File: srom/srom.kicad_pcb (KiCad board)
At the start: 2 copper layers, 83.3 x 76.1 mm, 18 parts, among them J1 Conn_01x03_Female, U1 4075, U2 74LS245, U3 74LS245, U4 74LS245, U5 Pico-rp2040

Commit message: minor updates to layout
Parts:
- added 1: , , F.Cu at (97.0, 118.9)
- added 10: , , F.Cu at (94.4, 124.0)
- added 11: , , F.Cu at (97.0, 124.0)
- added 12: , , F.Cu at (99.5, 124.0)
- added 13: , , F.Cu at (102.1, 116.3)
- added 13: , , F.Cu at (102.0, 124.0)
- added 14: , , F.Cu at (104.6, 116.3)
- added 14: , , F.Cu at (104.6, 124.0)
- added 2: , , F.Cu at (99.5, 118.9)
- added 3: , , F.Cu at (102.1, 111.2)
- added 3: , , F.Cu at (102.0, 118.9)
- added 4: , , F.Cu at (104.6, 111.2)
- added 4: , , F.Cu at (104.6, 118.9)
- added 5: , , F.Cu at (94.4, 121.4)
- added 6: , , F.Cu at (97.0, 121.4)
- added 7: , , F.Cu at (99.5, 121.4)
- added 8: , , F.Cu at (102.1, 113.8)
- added 8: , , F.Cu at (102.0, 121.4)
- added 9: , , F.Cu at (104.6, 121.4)
- added 9: , , F.Cu at (104.6, 113.8)
- added ?: , , F.Cu at (101.8, 54.6)
- added ?: , , F.Cu at (99.7, 52.6)
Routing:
- net unconnected-(U5-Pad32): track 0.00 -> 28.1 mm
- net unconnected-(U5-Pad34): track 0.00 -> 25.4 mm
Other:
- board text added: "GND"
- board text added: "GPIO27"
- board text added: "GPIO28"

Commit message: fab1.0 ready to go
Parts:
- added ?: , , F.Cu at (62.8, 107.2)
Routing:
- net GND: vias 18 -> 19
- added copper zone on F.Cu, net GND
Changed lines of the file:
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@@
       (layerselection 0x00010fc_ffffffff)
       (disableapertmacros false)
-      (usegerberextensions false)
-      (usegerberattributes true)
-      (usegerberadvancedattributes true)
-      (creategerberjobfile true)
+      (usegerberextensions true)
+      (usegerberattributes false)
+      (usegerberadvancedattributes false)
+      (creategerberjobfile false)
       (svguseinch false)
       (svgprecision 6)
@@
       (psa4output false)
       (plotreference true)
-      (plotvalue true)
+      (plotvalue false)
       (plotinvisibletext false)
       (sketchpadsonfab false)
-      (subtractmaskfromsilk false)
+      (subtractmaskfromsilk true)
       (outputformat 1)
       (mirror false)
-      (drillshape 1)
+      (drillshape 0)
       (scaleselection 1)
-      (outputdirectory "")
+      (outputdirectory "fab1.0")
     )
   )
@@
     (fp_line (start 1.6 0.8) (end -1.6 0.8) (layer "F.Fab") (width 0.1))
     (fp_line (start -1.6 -0.8) (end 1.6 -0.8) (layer "F.Fab") (width 0.1))
-    (pad "1" smd roundrect (at -1.475 0) (size 1.15 1.8) (layers "F.Cu" "F.Paste" "F.Mask") (roundrect_rratio 0.217391)
+    (pad "1" smd roundrect (at -1.475 0) (size 1.15 1.8) (layers "F.Cu" "F.Paste" "F.Mask") (roundrect_rratio 0.2173913043)
       (net 2 "GND") (pintype "passive"))
-    (pad "2" smd roundrect (at 1.475 0) (size 1.15 1.8) (layers "F.Cu" "F.Paste" "F.Mask") (roundrect_rratio 0.217391)
+    (pad "2" smd roundrect (at 1.475 0) (size 1.15 1.8) (layers "F.Cu" "F.Paste" "F.Mask") (roundrect_rratio 0.2173913043)
       (net 1 "+3V3") (pintype "passive"))
     (model "${KICAD6_3DMODEL_DIR}/Capacitor_SMD.3dshapes/C_1206_3216Metric.wrl"
@@
     (fp_line (start 1.6 0.8) (end -1.6 0.8) (layer "F.Fab") (width 0.1))
     (fp_line (start 1.6 -0.8) (end 1.6 0.8) (layer "F.Fab") (width 0.1))
-    (pad "1" smd roundrect (at -1.475 0 270) (size 1.15 1.8) (layers "F.Cu" "F.Paste" "F.Mask") (roundrect_rratio 0.217391)
+    (pad "1" smd roundrect (at -1.475 0 270) (size 1.15 1.8) (layers "F.Cu" "F.Paste" "F.Mask") (roundrect_rratio 0.2173913043)
       (net 3 "+5V") (pintype "passive"))
-    (pad "2" smd roundrect (at 1.475 0 270) (size 1.15 1.8) (layers "F.Cu" "F.Paste" "F.Mask") (roundrect_rratio 0.217391)
+    (pad "2" smd roundrect (at 1.475 0 270) (size 1.15 1.8) (layers "F.Cu" "F.Paste" "F.Mask") (roundrect_rratio 0.2173913043)
       (net 2 "GND") (pintype "passive"))
     (model "${KICAD6_3DMODEL_DIR}/Capacitor_SMD.3dshapes/C_1206_3216Metric.wrl"
@@
     (fp_line (start 1.6 -0.8) (end 1.6 0.8) (layer "F.Fab") (width 0.1))
     (fp_line (start -1.6 0.8) (end -1.6 -0.8) (layer "F.Fab") (width 0.1))
-    (pad "1" smd roundrect (at -1.475 0 180) (size 1.15 1.8) (layers "F.Cu" "F.Paste" "F.Mask") (roundrect_rratio 0.217391)
+    (pad "1" smd roundrect (at -1.475 0 180) (size 1.15 1.8) (layers "F.Cu" "F.Paste" "F.Mask") (roundrect_rratio 0.2173913043)
       (net 1 "+3V3") (pintype "passive"))
-    (pad "2" smd roundrect (at 1.475 0 180) (size 1.15 1.8) (layers "F.Cu" "F.Paste" "F.Mask") (roundrect_rratio 0.217391)
+    (pad "2" smd roundrect (at 1.475 0 180) (size 1.15 1.8) (layers "F.Cu" "F.Paste" "F.Mask") (roundrect_rratio 0.2173913043)
       (net 2 "GND") (pintype "passive"))
     (model "${KICAD6_3DMODEL_DIR}/Capacitor_SMD.3dshapes/C_1206_3216Metric.wrl"
@@
   )
   (footprint "" (layer "F.Cu")
+    (at 62.77 107.21)
+    (fp_text reference "" (at 0 0) (layer "F.SilkS")
+      (effects (font (size 1.27 1.27) (thickness 0.15)))
+    )
+    (fp_text value "" (at 0 0) (layer "F.SilkS")
+      (effects (font (size 1.27 1.27) (thickness 0.15)))
+    )
+    (pad "" thru_hole circle (at 0 0) (size 2 2) (drill 1) (layers *.Cu *.Mask)
+      (net 2 "GND"))
+  )
+  (footprint "" (layer "F.Cu")
     (at 99.73 52.6)
     (fp_text reference "" (at 0 0) (layer "F.SilkS")
@@
     (fp_line (start -1.6 -0.8) (end 1.6 -0.8) (layer "F.Fab") (width 0.1))
     (fp_line (start -1.6 0.8) (end -1.6 -0.8) (layer "F.Fab") (width 0.1))
-    (pad "1" smd roundrect (at -1.475 0 180) (size 1.15 1.8) (layers "F.Cu" "F.Paste" "F.Mask") (roundrect_rratio 0.217391)
+    (pad "1" smd roundrect (at -1.475 0 180) (size 1.15 1.8) (layers "F.Cu" "F.Paste" "F.Mask") (roundrect_rratio 0.2173913043)
       (net 1 "+3V3") (pintype "passive"))
-    (pad "2" smd roundrect (at 1.475 0 180) (size 1.15 1.8) (layers "F.Cu" "F.Paste" "F.Mask") (roundrect_rratio 0.217391)
+    (pad "2" smd roundrect (at 1.475 0 180) (size 1.15 1.8) (layers "F.Cu" "F.Paste" "F.Mask") (roundrect_rratio 0.2173913043)
       (net 2 "GND") (pintype "passive"))
     (model "${KICAD6_3DMODEL_DIR}/Capacitor_SMD.3dshapes/C_1206_3216Metric.wrl"
@@
   (gr_line (start 95.03 53.86) (end 95.53 53.52) (layer "F.SilkS") (width 0.15))
   (gr_line (start 95.03 53.18) (end 95.03 53.86) (layer "F.SilkS") (width 0.15))
+  (gr_rect (start 91.9 125.49) (end 70.19 123.34) (layer "B.Mask") (width 0.15) (fill solid))
+  (gr_rect (start 91.93 125.49) (end 70.21 123.57) (layer "F.Mask") (width 0.15) (fill solid))
   (gr_rect (start 23.18 49.98) (end 106.46 126.07) (layer "Edge.Cuts") (width 0.1) (fill none))
   (gr_text "GPIO28" (at 102.36 52.05) (layer "F.SilkS")
@@
   )
   (gr_text "ROM Acc\n3V3" (at 71.52 83.08) (layer "F.SilkS")
+    (effects (font (size 1 0.5) (thickness 0.125)))
+  )
+  (gr_text "GND" (at 60.55 107.29) (layer "F.SilkS")
     (effects (font (size 1 0.5) (thickness 0.125)))
   )
@@
   (via (at 72.48 80.34) (size 0.8) (drill 0.4) (layers "F.Cu" "B.Cu") (net 2))
   (via (at 41.29 88.31) (size 0.8) (drill 0.4) (layers "F.Cu" "B.Cu") (net 2))
+  (via (at 73.44 124.94) (size 0.8) (drill 0.4) (layers "F.Cu" "B.Cu") (free) (net 2))
   (via (at 58.31 54.81) (size 0.8) (drill 0.4) (layers "F.Cu" "B.Cu") (net 2))
   (via (at 71.69 112.51) (size 0.8) (drill 0.4) (layers "F.Cu" "B.Cu") (net 2))
@@
   (segment (start 101.94 57.39) (end 99.14 54.59) (width 0.25) (layer "B.Cu") (net 85))
   (segment (start 99.14 54.59) (end 99.14 53.19) (width 0.25) (layer "B.Cu") (net 85))
-  (segment (start 99.81 52.68) (end 99.73 52.6) (width 0.25) (layer "B.Cu") (net 85))
   (segment (start 99.14 53.19) (end 99.73 52.6) (width 0.25) (layer "B.Cu") (net 85))
   (segment (start 100.69 73.43) (end 101.94 72.18) (width 0.25) (layer "B.Cu") (net 85))
   (segment (start 98.13 73.43) (end 100.69 73.43) (width 0.25) (layer "B.Cu") (net 85))
+  (zone (net 2) (net_name "GND") (layers F&B.Cu) (hatch edge 0.508)
+    (connect_pads (clearance 0.508))
+    (min_thickness 0.254) (filled_areas_thickness no)
+    (fill yes (thermal_gap 0.508) (thermal_bridge_width 0.508))
+    (polygon
+      (pts
+        (xy 91.42 123.47)
+        (xy 91.42 126.43)
+        (xy 91.341525 125.611093)
+        (xy 70.219569 125.566897)
+        (xy 70.278044 123.455804)
+      )
+    )
+  )
+  (zone (net 2) (net_name "GND") (layers F&B.Cu) (hatch edge 0.508)
+    (connect_pads (clearance 0.508))
+    (min_thickness 0.254) (filled_areas_thickness no)
+    (fill yes (thermal_gap 0.508) (thermal_bridge_width 0.508))
+    (polygon
+      (pts
+        (xy 91.787252 125.538043)
+        (xy 70.257252 125.588043)
+        (xy 70.26 123.511551)
+        (xy 70.29 123.651551)
+        (xy 70.260167 123.461569)
+        (xy 91.790167 123.441569)
+      )
+    )
+  )
   (zone (net 2) (net_name "GND") (layer "B.Cu") (hatch edge 0.508)
     (connect_pads (clearance 0.508))

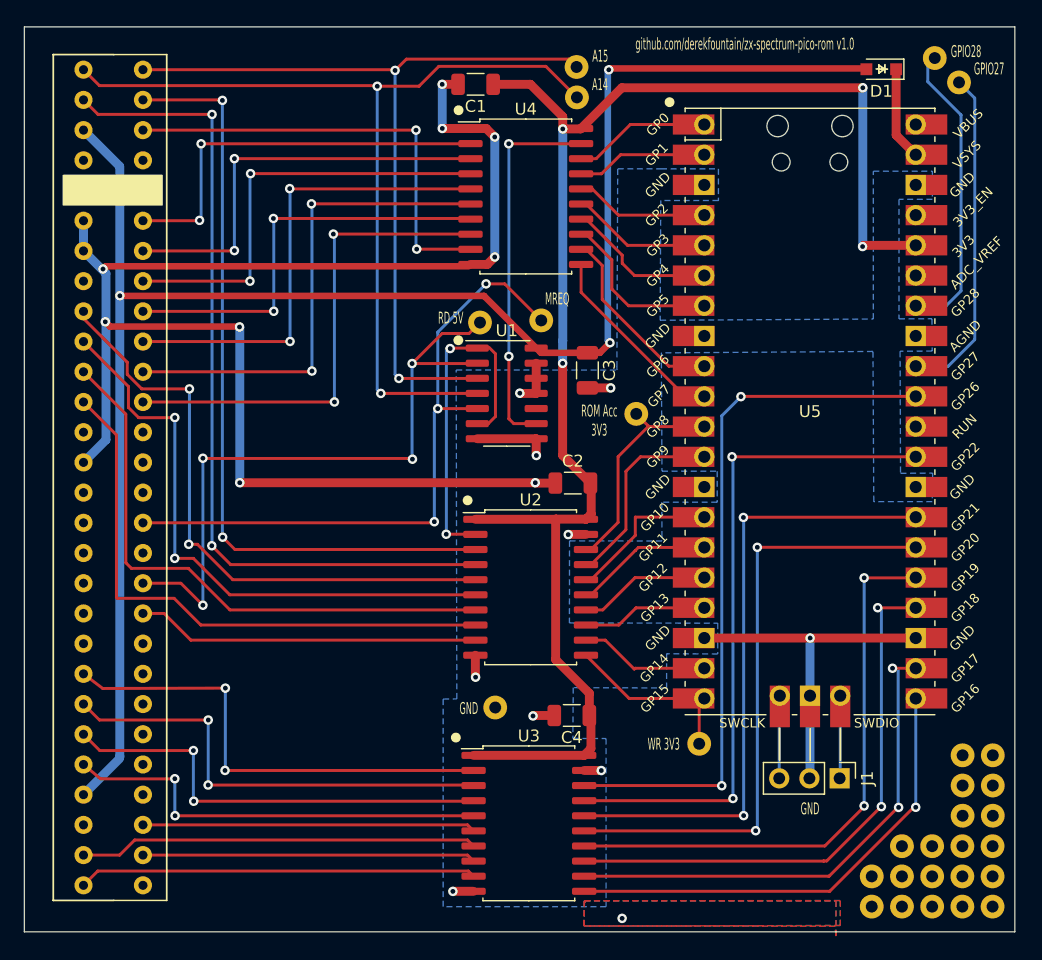
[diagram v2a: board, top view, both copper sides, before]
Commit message: update pcb with errata
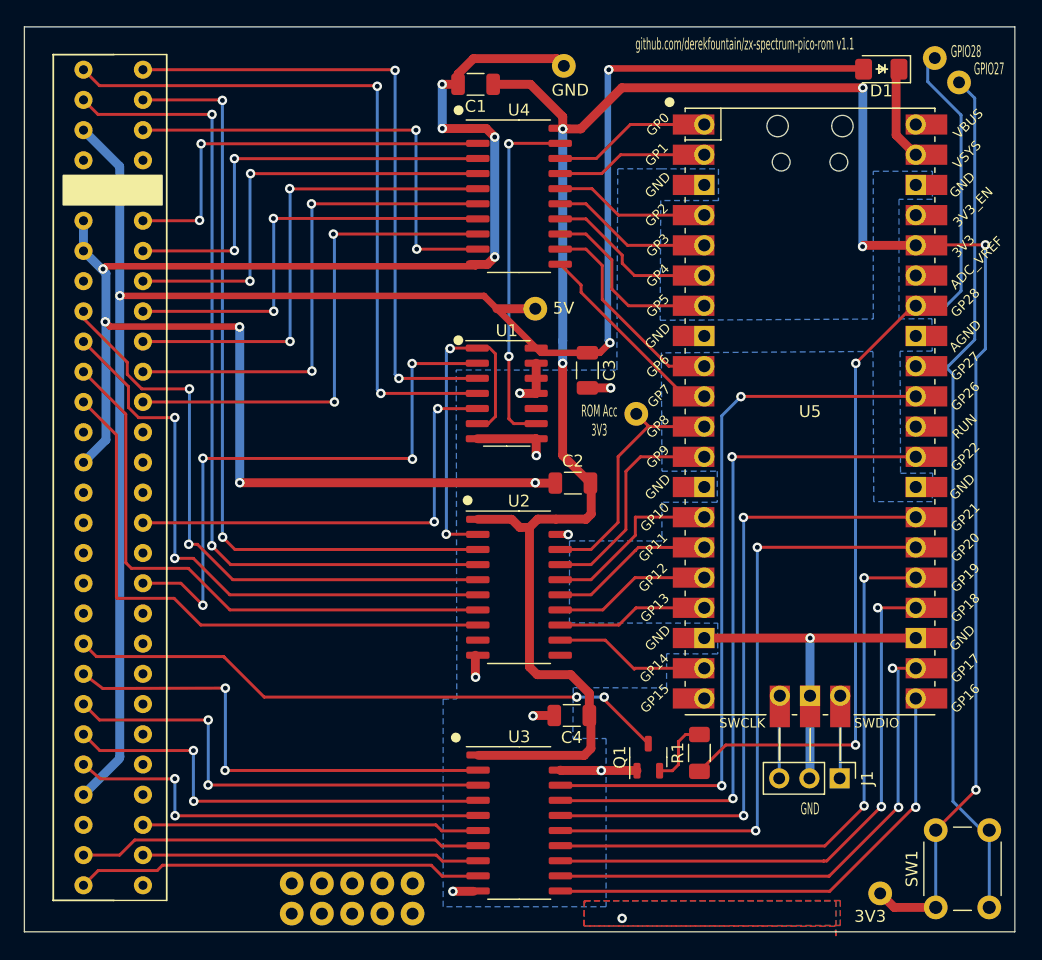
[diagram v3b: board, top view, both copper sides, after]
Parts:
- removed 1, 2, 3 (x2), 4 (x2): , 
- removed the 13 at (102.1, 116.3)
- removed the 14 at (104.6, 116.3)
- removed the 8 at (102.1, 113.8)
- removed the 9 at (104.6, 113.8)
- removed the ? at (61.5, 74.8)
- removed the ? at (66.6, 74.7)
- removed the ? at (69.6, 55.9)
- removed the ? at (62.8, 107.2)
- removed the ? at (79.9, 110.3)
- removed the ? at (69.6, 53.4)
- added 14: , , F.Cu at (95.1, 122.8)
- added 14: , , F.Cu at (68.5, 53.3)
- added ?: , , F.Cu at (66.1, 73.7)
- added Q1: PN2222A, Package_TO_SOT_SMD:SOT-23-3, F.Cu at (75.6, 111.4)
- added R1: 1K, Resistor_SMD:R_1206_3216Metric_Pad1.30x1.75mm_HandSolder, F.Cu at (79.9, 111.0)
- added SW1: SW_SPST, Button_Switch_THT:SW_PUSH_6mm_H4.3mm, F.Cu at (99.8, 124.0)
- D1: footprint Diode_SMD:D_SOD-323_HandSoldering -> Diode_SMD:D_1206_3216Metric_Pad1.42x1.75mm_HandSolder
- U2, U3, U4: footprint Package_SO:SOIC-20W_7.5x12.8mm_P1.27mm -> Package_SO:SO-20_5.3x12.6mm_P1.27mm
- moved 10 48.8 mm to (45.7, 124.5)
- moved 5 48.8 mm to (45.7, 122.0)
- moved 12 48.8 mm to (50.7, 124.5)
- moved 14 48.8 mm to (55.8, 124.5)
- moved 7 48.8 mm to (50.7, 122.0)
- moved 9 48.8 mm to (55.8, 122.0)
- moved 11 48.8 mm to (48.2, 124.5)
- moved 13 48.8 mm to (53.3, 124.5)
- moved 6 48.8 mm to (48.2, 122.0)
- moved 8 48.8 mm to (53.3, 122.0)
- moved U2 0.98 mm to (64.8, 97.1)
- moved U3 0.81 mm to (64.8, 116.9)
- moved U4 0.57 mm to (64.8, 64.2)
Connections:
- U2 pad 11: WR -> unconnected-(U2-Pad11)
- U2 pad 9: ZXWR -> unconnected-(U2-Pad9)
- U5 pad 20: WR -> unconnected-(U5-Pad20)
- U5 pad 32: unconnected-(U5-Pad32) -> PICO_USER_INPUT
- U5 pad 34: unconnected-(U5-Pad34) -> PICO_RESET_Z80
- Z1 pad A19: ZXWR -> unconnected-(Z1-PadA19)
- Z1 pad B20: unconnected-(Z1-PadB20) -> ZXRESET
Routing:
- net PICO_RESET_Z80: track 0.00 -> 77.7 mm, vias 0 -> 2
- net PICO_USER_INPUT: track 0.00 -> 75.5 mm
- net +3V3: track 126.5 -> 196.8 mm, vias 4 -> 6
- net ZXRESET: track 0.00 -> 51.1 mm, vias 0 -> 2
- net ZXWR: track 28.9 -> 0.00 mm
- net unconnected-(U5-Pad32): track 28.1 -> 0.00 mm
- net unconnected-(U5-Pad34): track 25.3 -> 0.00 mm
- net ZXA14: track 77.9 -> 59.3 mm
- net ZXMREQ: track 55.6 -> 37.5 mm, vias 3 -> 2
- net ZXA15: track 69.8 -> 53.9 mm
- net WR: track 15.4 -> 0.00 mm
- net GND: track 176.2 -> 191.6 mm
- net ZXRD: track 56.3 -> 49.1 mm
- net Net-(Q1-Pad2): track 0.00 -> 5.75 mm
- net +5V: track 146.7 -> 149.9 mm
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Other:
- board text added: "3V3"
- board text added: "5V"
- board text added: "github.com/derekfountain/zx-spectrum-pico-rom v1.1"
- board text removed: "A14"
- board text removed: "A15"
- board text removed: "MREQ"
- board text removed: "RD 5V"
- board text removed: "WR 3V3"
- board text removed: "github.com/derekfountain/zx-spectrum-pico-rom v1.0"

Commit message: add a ground plane on the back
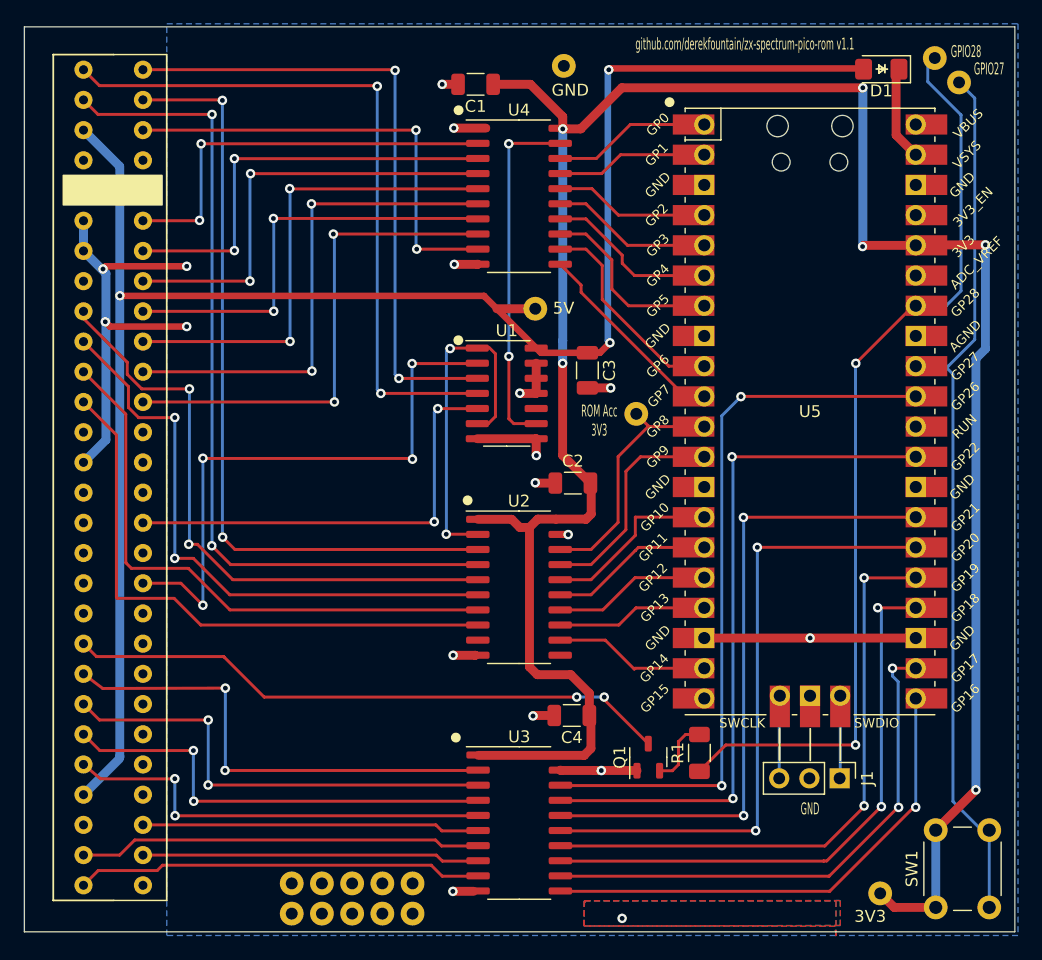
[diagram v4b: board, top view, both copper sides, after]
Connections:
- ? pad : unconnected-(U5-Pad32) -> PICO_USER_INPUT
- ? pad : unconnected-(U5-Pad34) -> PICO_RESET_Z80
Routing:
- net GND: track 191.6 -> 86.2 mm, vias 19 -> 18
